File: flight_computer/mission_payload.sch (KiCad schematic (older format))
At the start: 13 parts

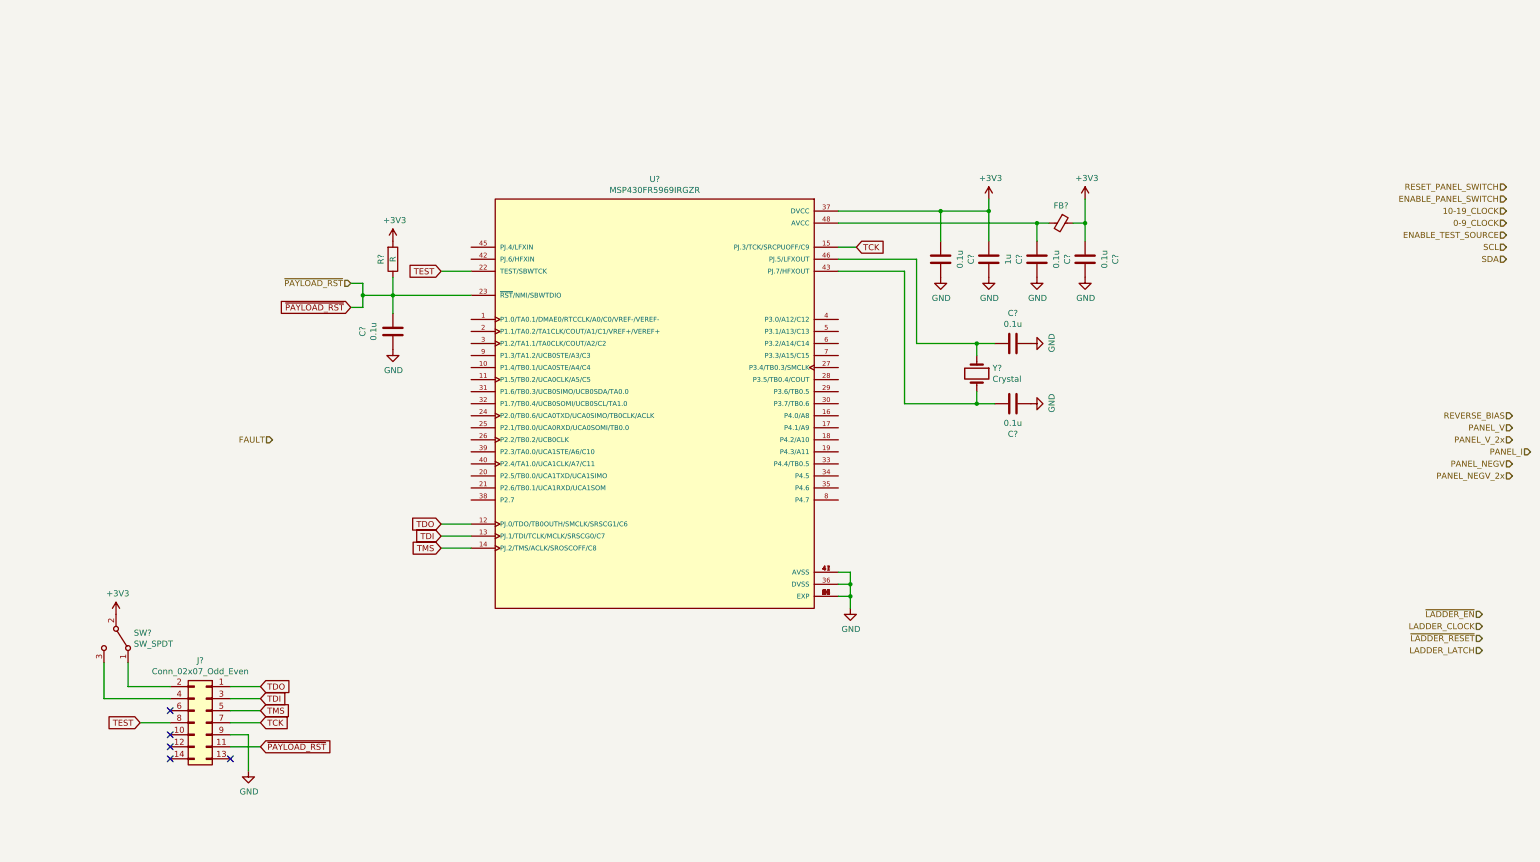
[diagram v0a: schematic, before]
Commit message: Updating flight computer
- Added datasheets for peripherals
- Added resistor ladder firmware
- Added perovskite switcher firmware
- Started flight computer firmware
- Added curve comparisons
- Updating flight computer schematic
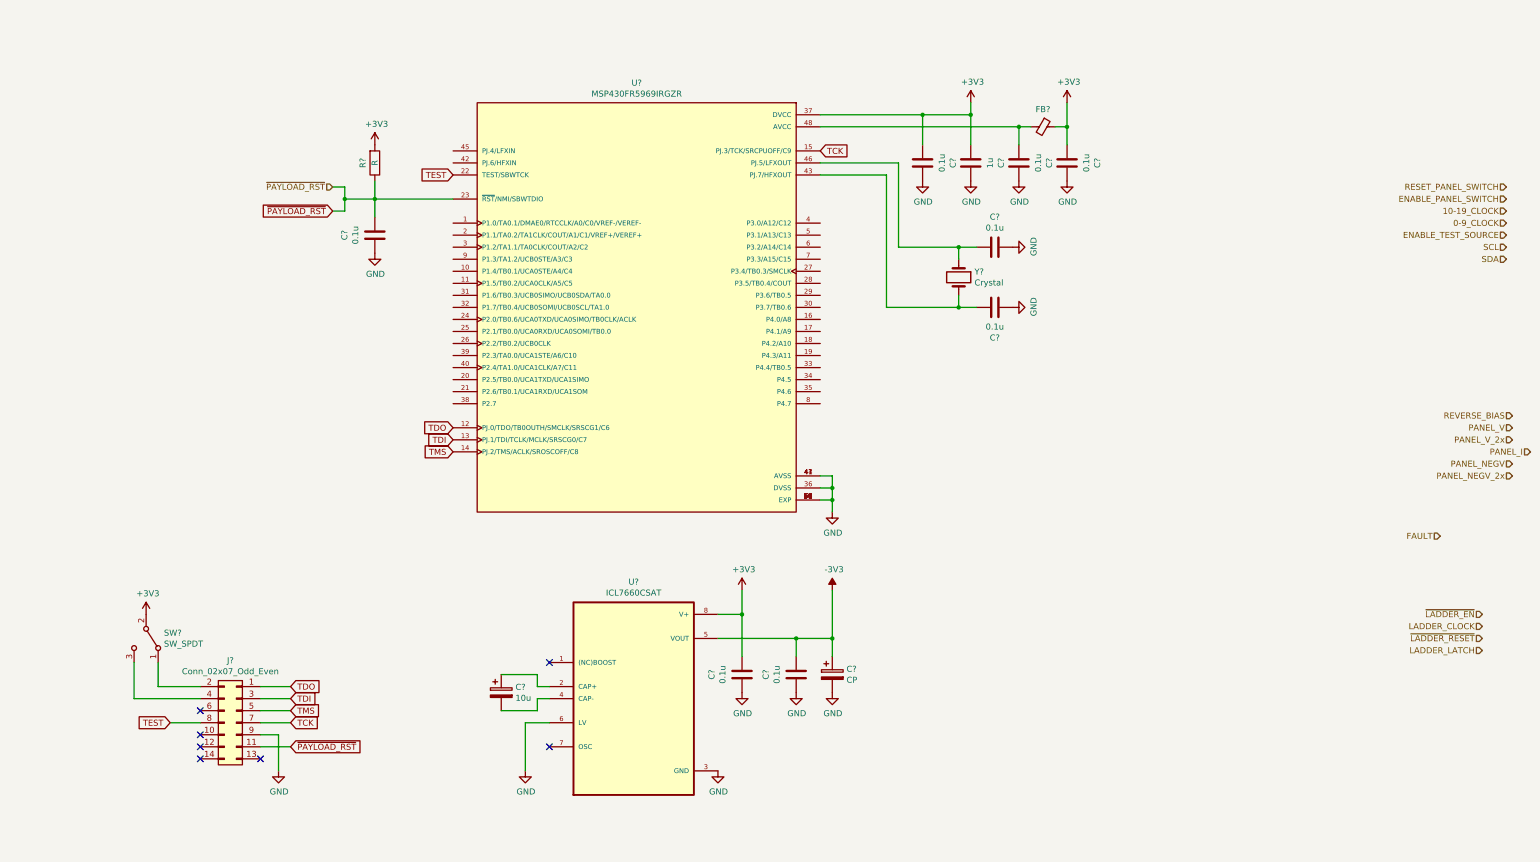
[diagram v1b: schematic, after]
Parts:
- added C?: CP, symbol Device:CP
- added C? (x2): 0.1u, Capacitor_SMD:C_0603_1608Metric, symbol Device:C
- added C?: 10u, symbol Device:CP
- added U?: ICL7660CSAT, SOIC127P600X175-8N, symbol ICL7660CSAT:ICL7660CSAT
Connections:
- net +3V3: now also C?.2, U?.8 (V+)
- net GND: now also C?.1, C?.1, C?.2, U?.3 (GND), U?.6 (LV)
- new net: C?.1, U?.2 (CAP+)
- new net: C?.2, U?.4 (CAP-)
- new net -3V3: C?.1, C?.2, U?.5 (VOUT)
- no-connect marks 5 -> 7
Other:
- moved on the sheet: C?, FB?, J?, R?, SW?, U?, Y?

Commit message: Update flight computer schematic
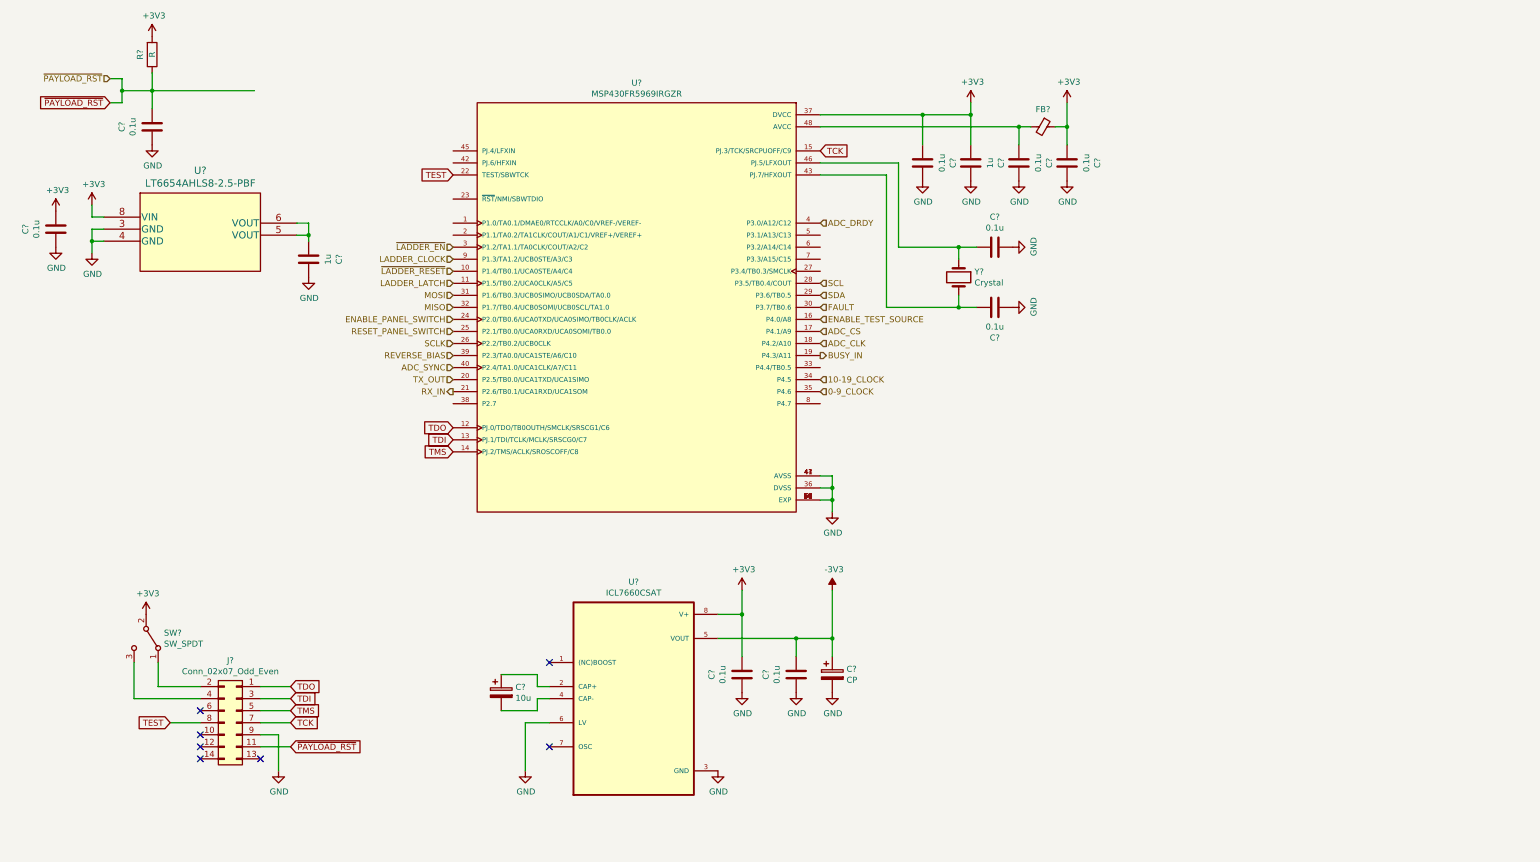
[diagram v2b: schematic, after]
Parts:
- added C?: 0.1u, Capacitor_SMD:C_0603_1608Metric, symbol Device:C
- added C?: 1u, Capacitor_SMD:C_0603_1608Metric, symbol Device:C
- added U?: LT6654AHLS8-2.5-PBF, LCC-8_LS8_LIT, symbol LT6654AHLS8-2.5-PBF:LT6654AHLS8-2.5-PBF
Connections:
- net +3V3: now also C?.2, U?.8 (VIN)
- net 0-9_CLOCK: now also U?.35 (P4.6)
- net 10-19_CLOCK: now also U?.34 (P4.5)
- net ENABLE_PANEL_SWITCH: now also U?.24 (P2.0/TB0.6/UCA0TXD/UCA0SIMO/TB0CLK/ACLK)
- net ENABLE_TEST_SOURCE: now also U?.16 (P4.0/A8)
- net FAULT: now also U?.30 (P3.7/TB0.6)
- net GND: now also C?.1, C?.2, U?.3 (GND), U?.4 (GND)
- net LADDER_CLOCK: now also U?.9 (P1.3/TA1.2/UCB0STE/A3/C3)
- net LADDER_LATCH: now also U?.11 (P1.5/TB0.2/UCA0CLK/A5/C5)
- net RESET_PANEL_SWITCH: now also U?.25 (P2.1/TB0.0/UCA0RXD/UCA0SOMI/TB0.0)
- net REVERSE_BIAS: now also U?.39 (P2.3/TA0.0/UCA1STE/A6/C10)
- net SCL: now also U?.28 (P3.5/TB0.4/COUT)
- net SDA: now also U?.29 (P3.6/TB0.5)
- net ~LADDER_EN: now also U?.3 (P1.2/TA1.1/TA0CLK/COUT/A2/C2)
- net ~LADDER_RESET: now also U?.10 (P1.4/TB0.1/UCA0STE/A4/C4)
- net ~PAYLOAD_RST: no longer U?.23 (~RST~/NMI/SBWTDIO)
- net ADC_CS: now reaches U?.17 (P4.1/A9)
- net ADC_CLK: now reaches U?.18 (P4.2/A10)
- net BUSY_IN: now reaches U?.19 (P4.3/A11)
- net TX_OUT: now reaches U?.20 (P2.5/TB0.0/UCA1TXD/UCA1SIMO)
- net RX_IN: now reaches U?.21 (P2.6/TB0.1/UCA1RXD/UCA1SOM)
- net SCLK: now reaches U?.26 (P2.2/TB0.2/UCB0CLK)
- net MOSI: now reaches U?.31 (P1.6/TB0.3/UCB0SIMO/UCB0SDA/TA0.0)
- net MISO: now reaches U?.32 (P1.7/TB0.4/UCB0SOMI/UCB0SCL/TA1.0)
- net ADC_DRDY: now reaches U?.4 (P3.0/A12/C12)
- net ADC_SYNC: now reaches U?.40 (P2.4/TA1.0/UCA1CLK/A7/C11)
- new net: C?.1, U?.5 (VOUT), U?.6 (VOUT)
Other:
- moved on the sheet: C?, R?

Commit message: Annotating schematic with references and footprints
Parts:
- removed Y?: Crystal, symbol Device:Crystal
- added Y?: CM8V-T1A, XTAL_CM8V-T1A-32.768KHZ-7PF-20PPM-TA-QC, symbol CM8V-T1A-32.768KHZ-7PF-20PPM-TA-QC:CM8V-T1A-32.768KHZ-7PF-20PPM-TA-QC
- C58, C59: renamed from C?; value 0.1u -> 10p
- U33: renamed from U?; footprint SOIC127P600X175-8N -> ICL7660CSAT:SOIC127P600X175-8N
- U34: renamed from U?; footprint QFN50P700X700X100-49N -> MSP430FR5969IRGZR:QFN50P700X700X100-49N
- gave numbers to parts that had none: 16
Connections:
- net ~PAYLOAD_RST: now also U34.23 (~RST~/NMI/SBWTDIO)
- net at C51.1, U32.5 (VOUT), U32.6 (VOUT): now also U34.2 (P1.1/TA0.2/TA1CLK/COUT/A1/C1/VREF+/VEREF+)
- net at C59.2, U34.43 (PJ.7/HFXOUT): now also Y?.2
- net at C58.2, U34.46 (PJ.5/LFXOUT): now also Y?.1
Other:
- moved on the sheet: C49, C50, C51, R57, U32

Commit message: Continuing layout
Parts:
- removed C49: 0.1u, Capacitor_SMD:C_0603_1608Metric, symbol Device:C
- removed C51: 1u, Capacitor_SMD:C_0603_1608Metric, symbol Device:C
- removed U32: LT6654AHLS8-2.5-PBF, LCC-8_LS8_LIT, symbol LT6654AHLS8-2.5-PBF:LT6654AHLS8-2.5-PBF
- added C44: 10u, Capacitor_SMD:C_0603_1608Metric, symbol Device:CP
- added C45: 0.1u, Capacitor_SMD:C_0603_1608Metric, symbol Device:C
- added J3: Conn_01x08_Female, Connector_PinSocket_2.54mm:PinSocket_1x08_P2.54mm_Vertical, symbol Connector:Conn_01x08_Female
- C52, C55: footprint (none) -> Capacitor_SMD:C_0603_1608Metric
- FB2: footprint (none) -> Inductor_SMD:L_0603_1608Metric
- J4: footprint (none) -> Connector_PinSocket_2.54mm:PinSocket_2x08_P2.54mm_Vertical
- SW2: footprint (none) -> Button_Switch_SMD:SW_SPDT_PCM12
- Y1: renamed from Y?; footprint XTAL_CM8V-T1A-32.768KHZ-7PF-20PPM-TA-QC -> CM8V-T1A-32:XTAL_CM8V-T1A-32.768KHZ-7PF-20PPM-TA-QC
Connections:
- net +3V3: now also C44.1, C45.2, J3.7 (Pin_7), J3.8 (Pin_8)
- net -3V3: now also C55.2; no longer C55.1
- net FAULT: now also J3.5 (Pin_5)
- net GND: now also C55.1, C44.2, C45.1, J3.1 (Pin_1), J3.2 (Pin_2); no longer C55.2
- net RX_IN: now also J3.4 (Pin_4)
- net TX_OUT: now also J3.3 (Pin_3)
- net ~PAYLOAD_RST: no longer C50.2, R57.1, U34.23 (~RST~/NMI/SBWTDIO)
- new net PAYLOAD_RST: C50.2, J3.6 (Pin_6), R57.1, U34.23 (~RST~/NMI/SBWTDIO)
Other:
- moved on the sheet: C50, J4, R57, SW2
